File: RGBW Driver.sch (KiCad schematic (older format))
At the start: 25 parts, among them J1 LED, J2 LED, J3 LED, J4 LED, J5 Power, U1 PT4115, U2 PT4115, U3 PT4115, U4 PT4115

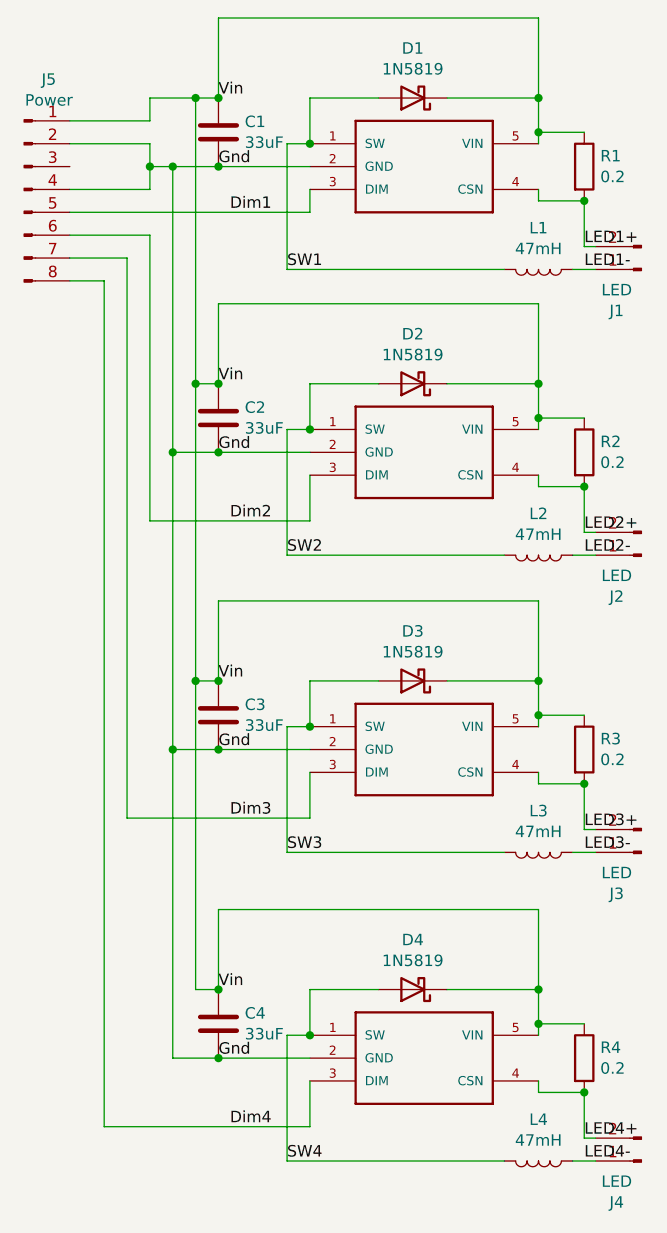
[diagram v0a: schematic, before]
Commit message: Place-replicate the layout
also replaced some trackign with filled zones.
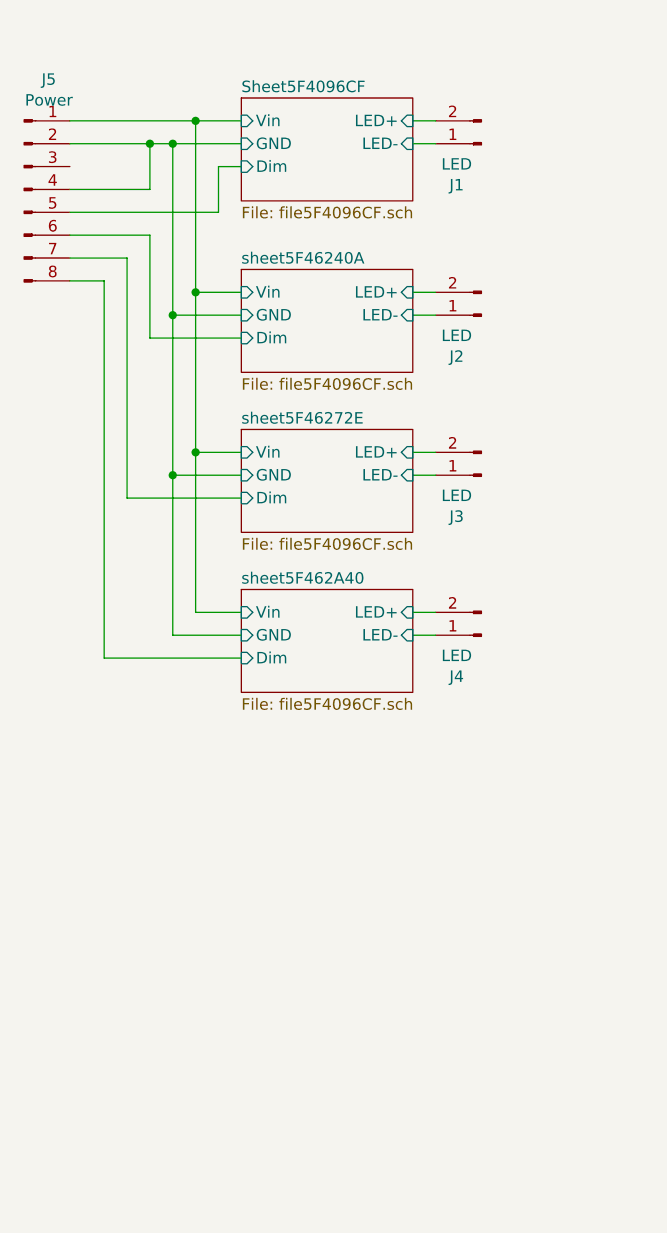
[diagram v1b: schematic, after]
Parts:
- removed C1, C2, C3, C4: 33uF, Capacitors_SMD:C_1210, symbol Device:C
- removed D1, D2, D3, D4: 1N5819, Diodes_SMD:D_SOD-123, symbol Diode:1N5819
- removed L1, L2, L3, L4: 47mH, Inductors_SMD:L_12x12mm_h6mm, symbol Device:L
- removed R1, R2, R3, R4: 0.2, Resistors_SMD:R_1206, symbol Device:R
- removed U1, U2, U3, U4: PT4115, TO_SOT_Packages_SMD:SOT-89-5_Housing, symbol PT4115:PT4115
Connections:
- net Dim1 renamed Sheet5F4096CF/Dim
- net Dim2 renamed sheet5F46240A/Dim
- net Dim3 renamed sheet5F46272E/Dim
- net Dim4 renamed sheet5F462A40/Dim
- net Gnd renamed Sheet5F4096CF/GND
- net LED1+ renamed Sheet5F4096CF/LED+
- net LED1- renamed Sheet5F4096CF/LED-
- net LED2+ renamed sheet5F46240A/LED+
- net LED2- renamed sheet5F46240A/LED-
- net LED3+ renamed sheet5F46272E/LED+
- net LED3- renamed sheet5F46272E/LED-
- net LED4+ renamed sheet5F462A40/LED+
- net LED4- renamed sheet5F462A40/LED-
- net Vin renamed Sheet5F4096CF/Vin
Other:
- moved on the sheet: J1, J2, J3, J4
